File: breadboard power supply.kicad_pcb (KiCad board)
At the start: 2 copper layers, 62.9 x 61.1 mm, 27 parts, among them J1 Screw_Terminal_01x02, J10 Conn_01x03_Male, J11 Barrel_Jack_Switch, J12 Conn_01x02_Male, J13 Screw_Terminal_01x02, J2 USB_B, J3 Conn_01x03_Male, J4 Conn_01x03_Male, J5 Conn_01x02_Male, J6 Conn_01x03_Male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

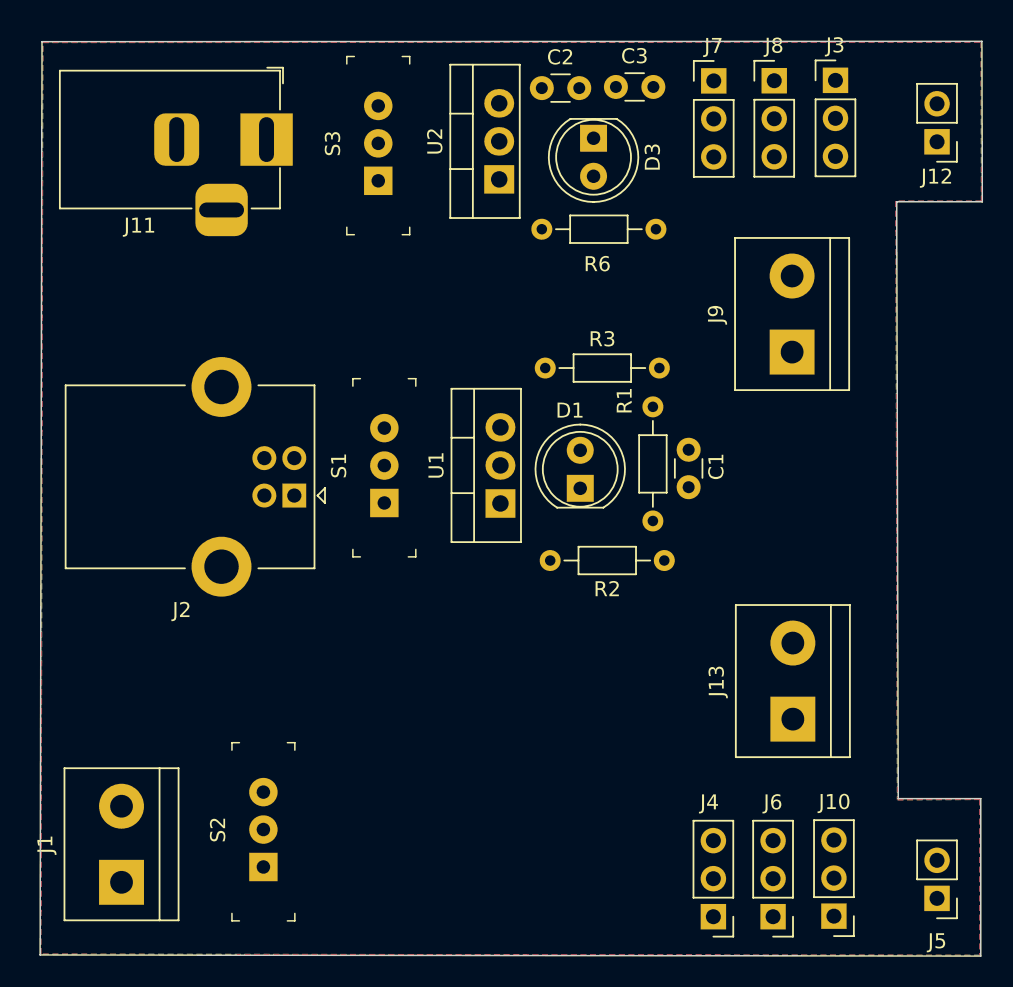
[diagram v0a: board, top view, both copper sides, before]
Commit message: board autorouted.
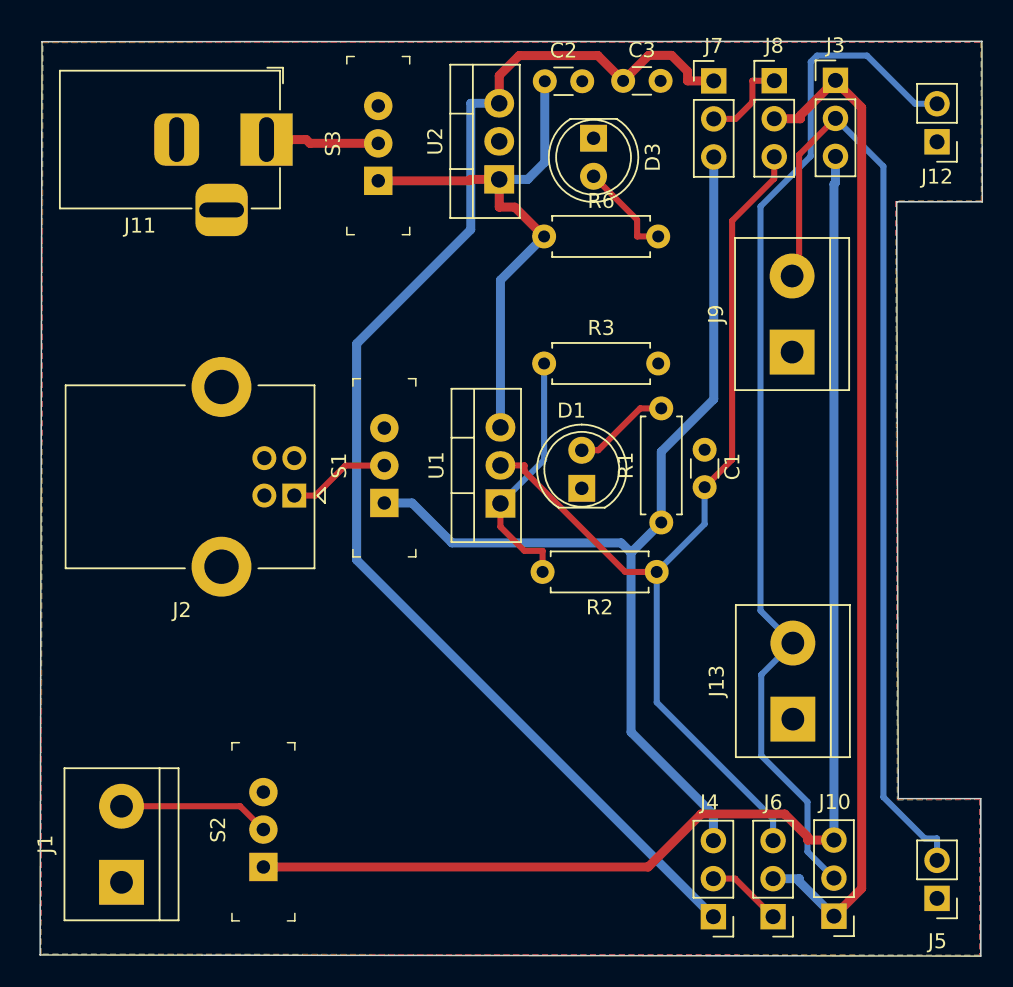
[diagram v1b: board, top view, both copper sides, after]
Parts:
- R1, R2, R3, R6: footprint Resistor_THT:R_Axial_DIN0204_L3.6mm_D1.6mm_P7.62mm_Horizontal -> Resistor_THT:R_Axial_DIN0207_L6.3mm_D2.5mm_P7.62mm_Horizontal
- moved C1 1.07 mm to (194.9, 77.6)
- moved R2 0.92 mm to (191.7, 83.3)
- moved C3 0.63 mm to (189.4, 50.5)
- moved R1 0.57 mm to (192.0, 80.0)
- moved R6 0.51 mm to (184.2, 60.9)
- moved C2 0.50 mm to (184.2, 50.5)
- moved R3 0.31 mm to (184.2, 69.3)
- moved D1 0.10 mm to (186.7, 77.7)
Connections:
- J10 pad 1: /V_USB/Regulator -> /V_Regulator/USB
- J3 pad 1: /V_USB/Regulator -> /V_Regulator/USB
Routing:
- net /5V_Regulator: track 0.00 -> 88.5 mm
- net /V_ScrewTerminal: track 0.00 -> 86.1 mm
- net Net-(J10-Pad2): track 0.00 -> 69.6 mm
- net /5V_USB: track 0.00 -> 68.1 mm
- net /V_Regulator/USB: track 0.00 -> 67.8 mm
- net /3V3_Regulator: track 0.00 -> 65.7 mm
- net Net-(J3-Pad2): track 0.00 -> 64.6 mm
- net /12V_BarrelJack: track 0.00 -> 36.7 mm
- net Net-(R2-Pad2): track 0.00 -> 17.0 mm
- net Net-(J1-Pad2): track 0.00 -> 10.1 mm
- net Net-(J11-Pad1): track 0.00 -> 7.57 mm
- net Net-(J2-Pad1): track 0.00 -> 6.84 mm
- net Net-(D3-Pad2): track 0.00 -> 6.63 mm
- net Net-(D1-Pad2): track 0.00 -> 6.47 mm
- net Net-(J7-Pad2): track 0.00 -> 5.93 mm
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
